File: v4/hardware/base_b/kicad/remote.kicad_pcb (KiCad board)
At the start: 2 copper layers, 111.8 x 100.3 mm, 31 parts, among them J12 Conn_01x04_Female, J16 Conn_01x04_Female, J19 Conn_01x03_Female, J2 Conn_01x12_Female, J20 Conn_01x04_Female, J3 Conn_01x16_Female, J5 Conn_01x03_Female, Q1 Q_NMOS_GDS, Q3 Q_NPN_EBC, SW1 SW_Push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

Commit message: update
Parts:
- removed J2: Conn_01x12_Female, Connector_PinSocket_2.54mm:PinSocket_1x12_P2.54mm_Vertical
- removed J3: Conn_01x16_Female, Connector_PinSocket_2.54mm:PinSocket_1x16_P2.54mm_Vertical
- removed gps1: Conn_01x04_Female, footprints:gps_neo6_blue_0
- removed sharp1: Conn_01x09_Female, footprints:Display_adafruit_sharp_13
- added AE1: Antenna_Shield, Connector_Coaxial:SMA_Amphenol_132289_EdgeMount, F.Cu at (-16.5, -20.3)
- added R7: 4.7K, Resistor_THT:R_Axial_DIN0309_L9.0mm_D3.2mm_P12.70mm_Horizontal, F.Cu at (44.5, 20.3)
- added SW3: SW_Push, Button_Switch_THT:SW_Tactile_SPST_Angled_PTS645Vx58-2LFS, F.Cu at (17.8, 8.89)
- added U3: Adafruit_IMU_BNO005, footprints:IMU_Ada_BNO005, F.Cu at (-16.5, 3.81)
- added U4: Adafruit_Sharp_Display_1_3, footprints:Display_adafruit_sharp_13, F.Cu at (0.00, 41.9)
- added U5: neo-6m-black, footprints:gps_neo6m_black, F.Cu at (-15.2, 36.8)
- moved H6 190.8 mm to (-27.9, -19.1)
- moved J5 164.4 mm to (-29.2, 14.0)
- moved H2 155.5 mm to (17.8, -19.1)
- moved H1 135.7 mm to (-29.2, 72.4)
- moved SW1 134.3 mm to (17.8, -11.4), turned to 270 degrees
- moved SW2 125.2 mm to (17.8, -1.27), turned to 270 degrees
- moved J16 101.1 mm to (19.1, 26.7)
- moved H5 96.6 mm to (19.1, 72.4)
- moved U1 91.6 mm to (-1.27, 0.00), turned to 180 degrees
- moved U2 5.24 mm to (14.0, 47.0), turned to 270 degrees
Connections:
- J5 pad 2: EN -> (no net)
- U2 pad 11: (no net) -> SCL
- U2 pad 12: (no net) -> SDA
- U2 pad 17: (no net) -> A0
- U2 pad 20: (no net) -> A3
- U2 pad 21: (no net) -> A4
- U2 pad 22: (no net) -> A5
- U2 pad 26: (no net) -> RX_D0
- U2 pad 27: (no net) -> TX_D1
- U2 pad 28: (no net) -> DW
- U2 pad 8: (no net) -> D9
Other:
- board size 111.8 x 100.3 mm -> 53.3 x 97.8 mm

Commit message: update
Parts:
- removed AE1: Antenna_Shield, Connector_Coaxial:SMA_Amphenol_132289_EdgeMount
- added J1: Conn_Coaxial, Connector_Coaxial:SMA_Amphenol_132134_Vertical, F.Cu at (-14.0, -21.6)
- moved J20 176.5 mm to (-27.9, -1.27), turned to 270 degrees
- moved J12 172.8 mm to (-27.9, -11.4), turned to 270 degrees
- moved J19 154.6 mm to (-21.6, 72.4), turned to 90 degrees
- moved SP1 149.9 mm to (7.62, -8.89), turned to 90 degrees
- moved SW4 138.4 mm to (-30.5, 35.6), turned to 90 degrees
- moved R4 129.9 mm to (-24.1, 63.5), turned to 90 degrees
- moved R6 119.1 mm to (-29.2, 63.5), turned to 90 degrees
- moved R3 115.0 mm to (-8.89, 63.5), turned to 90 degrees
- moved Q3 113.1 mm to (19.1, 39.4), turned to 180 degrees
- moved JP1 104.7 mm to (6.74, 26.3), turned to 270 degrees
- moved JP3 103.7 mm to (6.74, 22.0), turned to 270 degrees
- moved R8 102.1 mm to (-19.1, 63.5), turned to 90 degrees
- moved Q1 96.2 mm to (19.1, 31.8), turned to 180 degrees
- moved R2 90.1 mm to (-14.0, 63.5), turned to 90 degrees
- moved R1 89.7 mm to (-3.81, 63.5), turned to 90 degrees
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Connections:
- U1 pad 9: (no net) -> Net-(J1-Pad1)
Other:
- board size 53.3 x 97.8 mm -> 53.3 x 100.3 mm

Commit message: update
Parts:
- removed J12: Conn_01x04_Female, Connector_JST:JST_SH_SM04B-SRSS-TB_1x04-1MP_P1.00mm_Horizontal
- removed JP3: Jumper_NO_Small, Jumper:SolderJumper-2_P1.3mm_Open_Pad1.0x1.5mm
- added J2: Conn_01x06_Female, Connector_PinHeader_2.54mm:PinHeader_1x06_P2.54mm_Vertical, F.Cu at (-26.5, 19.1)
- added J3: Conn_01x04_Female, Connector_JST:JST_SH_SM04B-SRSS-TB_1x04-1MP_P1.00mm_Horizontal, F.Cu at (-28.1, -11.9)
- added JP2: Jumper_NO_Small, Jumper:SolderJumper-2_P1.3mm_Open_Pad1.0x1.5mm, B.Cu at (-21.5, -1.14)
- Q1: footprint Package_TO_SOT_THT:TO-220-3_Vertical -> Package_TO_SOT_THT:TO-220-3_Horizontal_TabDown
- moved Q3 63.9 mm to (-8.22, -18.4), turned to 90 degrees
- moved J5 50.4 mm to (19.4, 27.0)
- moved SW4 42.0 mm to (-14.7, 74.5), turned to 180 degrees
- moved J16 34.0 mm to (-14.3, 7.56), turned to 90 degrees
- moved Q1 31.6 mm to (5.52, 3.24), turned to 0 degrees
- moved J19 20.7 mm to (-0.98, 73.8), turned to 270 degrees
- moved SP1 15.7 mm to (-2.72, -20.7), turned to 270 degrees
- moved H2 10.1 mm to (17.8, -21.6)
- moved SW1 8.12 mm to (18.3, -13.7)
- moved SW2 8.12 mm to (18.3, -3.52)
- moved SW3 8.12 mm to (18.3, 6.64)
- moved R6 6.35 mm to (-22.9, 63.5)
- moved R4 5.41 mm to (-18.7, 63.5)
- moved R8 4.46 mm to (-14.6, 63.5)
- moved R2 3.52 mm to (-10.5, 63.5)
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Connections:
- J19 pad 3: A3 -> A5
- J5 pad 2: (no net) -> EN
- R3 pad 2: A5 -> A3
- R4 pad 2: A4 -> A2
- R7 pad 2: A2 -> A4
- R8 pad 2: A0 -> A1
- SW1 pad 1: A4 -> A2
- SW2 pad 1: A5 -> A3
- SW3 pad 1: A2 -> A4
- U1 pad 14: (no net) -> D9
- U1 pad 15: (no net) -> Net-(JP2-Pad1)
- U1 pad 2: (no net) -> MISO
- U1 pad 3: (no net) -> MOSI
- U1 pad 4: (no net) -> SCK
- U1 pad 5: (no net) -> D5
- U1 pad 6: (no net) -> D6
- U2 pad 10: (no net) -> D5
- U2 pad 13: (no net) -> ~RESET
- U2 pad 14: (no net) -> +3V3
- U2 pad 16: (no net) -> GND
- U2 pad 18: (no net) -> A1
- U2 pad 19: (no net) -> A2
- U2 pad 2: (no net) -> EN
- U2 pad 23: (no net) -> SCK
- U2 pad 24: (no net) -> MOSI
- U2 pad 25: (no net) -> MISO
- U2 pad 28: DW -> (no net)
- U2 pad 4: (no net) -> D13
- U2 pad 5: (no net) -> D12
- U2 pad 6: (no net) -> D11
- U2 pad 7: (no net) -> D10
- U2 pad 9: (no net) -> D6
- U4 pad 4: (no net) -> SCK
- U4 pad 5: (no net) -> MOSI
- U4 pad 6: (no net) -> A0
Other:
- board size 53.3 x 100.3 mm -> 53.3 x 115.3 mm
- board text added: "JST"

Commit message: update
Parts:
- JP1: moved to B.Cu
- moved J3 69.6 mm to (-28.2, 57.7)
- moved Q3 58.0 mm to (-26.9, 36.6)
- moved R1 23.2 mm to (-21.7, 50.9), turned to 270 degrees
- moved R4 17.3 mm to (-1.43, 63.6)
- moved R8 17.2 mm to (2.63, 63.6)
- moved R2 14.5 mm to (-17.7, 50.9), turned to 270 degrees
- moved SP1 13.3 mm to (10.6, -21.0), turned to 180 degrees
- moved JP2 11.5 mm to (-10.4, -4.26), turned to 90 degrees
- moved R7 11.5 mm to (-9.55, 63.6)
- moved R6 9.26 mm to (-13.6, 63.6)
- moved U3 6.30 mm to (-23.7, 1.96)
- moved J20 5.69 mm to (-28.3, -7.11)
- moved SW2 4.91 mm to (15.3, 0.39)
- moved SW3 4.75 mm to (15.3, 10.4)
- moved J2 4.21 mm to (-27.5, 15.0)
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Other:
- outline, holes or cut-outs redrawn

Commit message: update
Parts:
- moved D2 12.7 mm to (11.8, 51.5), turned to 270 degrees
- moved SP1 3.77 mm to (6.82, -20.9)
- moved SW1 0.25 mm to (15.1, -13.4)
- moved SW2 0.23 mm to (15.1, 0.39)
- moved SW3 0.23 mm to (15.1, 10.4)
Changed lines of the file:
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@@
   )
   (module Button_Switch_THT:SW_Tactile_SPST_Angled_PTS645Vx58-2LFS (layer F.Cu)
-    (at 15.33144 10.3505 270)
+    (at 15.10538 10.3505 270)
     (descr "tactile switch SPST right angle, PTS645VL58-2 LFS")
     (tags "tactile switch SPST angled PTS645VL58-2 LFS C&K Button")
@@
   )
   (module Button_Switch_THT:SW_Tactile_SPST_Angled_PTS645Vx58-2LFS (layer F.Cu)
-    (at 15.33144 0.3937 270)
+    (at 15.10538 0.3937 270)
     (descr "tactile switch SPST right angle, PTS645VL58-2 LFS")
     (tags "tactile switch SPST angled PTS645VL58-2 LFS C&K Button")
@@
   )
   (module Button_Switch_THT:SW_Tactile_SPST_Angled_PTS645Vx58-2LFS (layer F.Cu)
-    (at 15.3543 -13.41628 270)
+    (at 15.10538 -13.41628 270)
     (descr "tactile switch SPST right angle, PTS645VL58-2 LFS")
     (tags "tactile switch SPST angled PTS645VL58-2 LFS C&K Button")
@@
   )
   (module "Adafruit Circuit Playground:BUZZER_SMT_5MM" (layer F.Cu)
-    (at 10.58926 -20.98802 180)
+    (at 6.81736 -20.8788 180)
     (fp_text reference SP1 (at 0 0) (layer F.SilkS) hide
       (effects (font (size 1.27 1.27) (thickness 0.15)))
@@
   )
   (module Diode_THT:D_5W_P12.70mm_Horizontal (layer F.Cu)
-    (at 11.71702 64.20612 90)
+    (at 11.81354 51.51374 270)
     (descr "Diode, 5W series, Axial, Horizontal, pin pitch=12.7mm, , length*diameter=8.9*3.7mm^2, , http://www.diodes.com/_files/packages/8686949.gif")
     (tags "Diode 5W series Axial Horizontal pin pitch 12.7mm  length 8.9mm diameter 3.7mm")
@@
     (fp_line (start 14.35 2.1) (end 14.35 -2.1) (layer F.CrtYd) (width 0.05))
     (fp_line (start 14.35 -2.1) (end -1.65 -2.1) (layer F.CrtYd) (width 0.05))
-    (pad 1 thru_hole rect (at 0 0 90) (size 2.8 2.8) (drill 1.4) (layers *.Cu *.Mask)
+    (pad 1 thru_hole rect (at 0 0 270) (size 2.8 2.8) (drill 1.4) (layers *.Cu *.Mask)
       (net 3 +3V3))
-    (pad 2 thru_hole oval (at 12.7 0 90) (size 2.8 2.8) (drill 1.4) (layers *.Cu *.Mask)
+    (pad 2 thru_hole oval (at 12.7 0 270) (size 2.8 2.8) (drill 1.4) (layers *.Cu *.Mask)
       (net 2 "Net-(D2-Pad2)"))
     (model ${KISYS3DMOD}/Diode_THT.3dshapes/D_5W_P12.70mm_Horizontal.wrl

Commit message: nice board layout for v4 base_b
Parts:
- removed the R5 at (6.68, 63.6)
- removed the R6 at (-13.6, 63.6)
- added R3: 10K, Resistor_THT:R_Axial_DIN0309_L9.0mm_D3.2mm_P12.70mm_Horizontal, F.Cu at (-10.9, 63.9)
- moved H5 94.1 mm to (17.8, -21.8)
- moved H2 93.5 mm to (17.8, 71.9)
- moved R1 2.68 mm to (-19.1, 51.2)
- moved R4 2.68 mm to (-6.89, 63.9)
- moved R5 2.68 mm to (-2.83, 63.9)
- moved R6 2.68 mm to (1.23, 63.9)
- moved R7 2.68 mm to (5.29, 63.9)
- moved R2 2.68 mm to (-15.0, 51.2)
- moved SW1 1.87 mm to (15.2, -15.3)
- moved J2 1.40 mm to (-26.1, 14.9)
- moved SW2 1.10 mm to (15.3, -0.69)
- moved SW3 1.10 mm to (15.3, 9.27)
- moved SW4 1.03 mm to (-12.9, 74.6)
- moved D1 0.80 mm to (11.1, 51.8)
- moved J16 0.64 mm to (-14.4, 6.93)
- renumbered D2 to D1, R7 to R4, R3 to R5, R4 to R6, R8 to R7
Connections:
- J19 pad 2: Net-(J19-Pad2) -> GND
- U3 pad 1: (no net) -> +3V3
- U3 pad 3: (no net) -> GND
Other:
- outline, holes or cut-outs redrawn
- board text added: "3.7V"
- board text added: "3V"
- board text added: "3V3"
- board text added: "A"
- board text added: "A1"
- board text added: "ANT"
- board text added: "ANTENNA"
- board text added: "B"
- board text added: "C"
- board text added: "D11"
- board text added: "D12"
- board text added: "D13"
- board text added: "G1"
- board text added: "GND"
- board text added: "GPS"
- board text added: "IMU"
- board text added: "LOG"
- board text added: "OFF"
- board text added: "ON"
- board text added: "PROG"
- board text added: "RESET"
- board text added: "RFM95"
- board text added: "RX_DO"
- board text added: "SCL"
- board text added: "SDA"
- board text added: "Sharp display"
- board text added: "Sharp display breakout"
- board text added: "TX_D1"

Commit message: update
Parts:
- Q1: footprint Package_TO_SOT_THT:TO-220-3_Horizontal_TabDown -> Package_TO_SOT_THT:TO-220-3_Horizontal_TabUp
- moved Q1 4.86 mm to (7.53, 3.15), turned to 180 degrees
- moved D1 0.98 mm to (10.1, 51.9)
- moved R1 0.72 mm to (-19.8, 51.3)
- moved R2 0.72 mm to (-15.7, 51.3)
- moved R3 0.72 mm to (-11.7, 64.0)
- moved R7 0.72 mm to (4.57, 64.0)
- moved R5 0.72 mm to (-3.55, 64.0)
- moved R6 0.72 mm to (0.51, 64.0)
- moved R4 0.72 mm to (-7.61, 64.0)

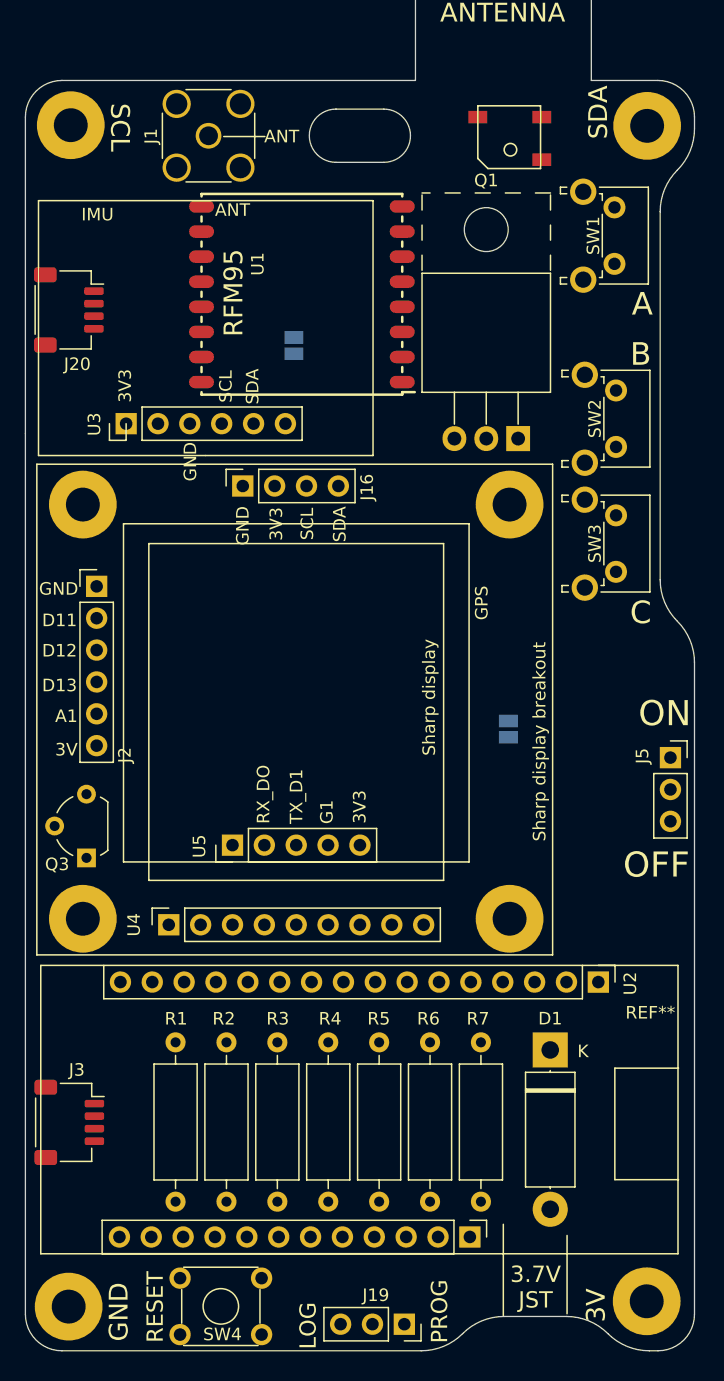
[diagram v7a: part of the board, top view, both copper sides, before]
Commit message: routed power lines
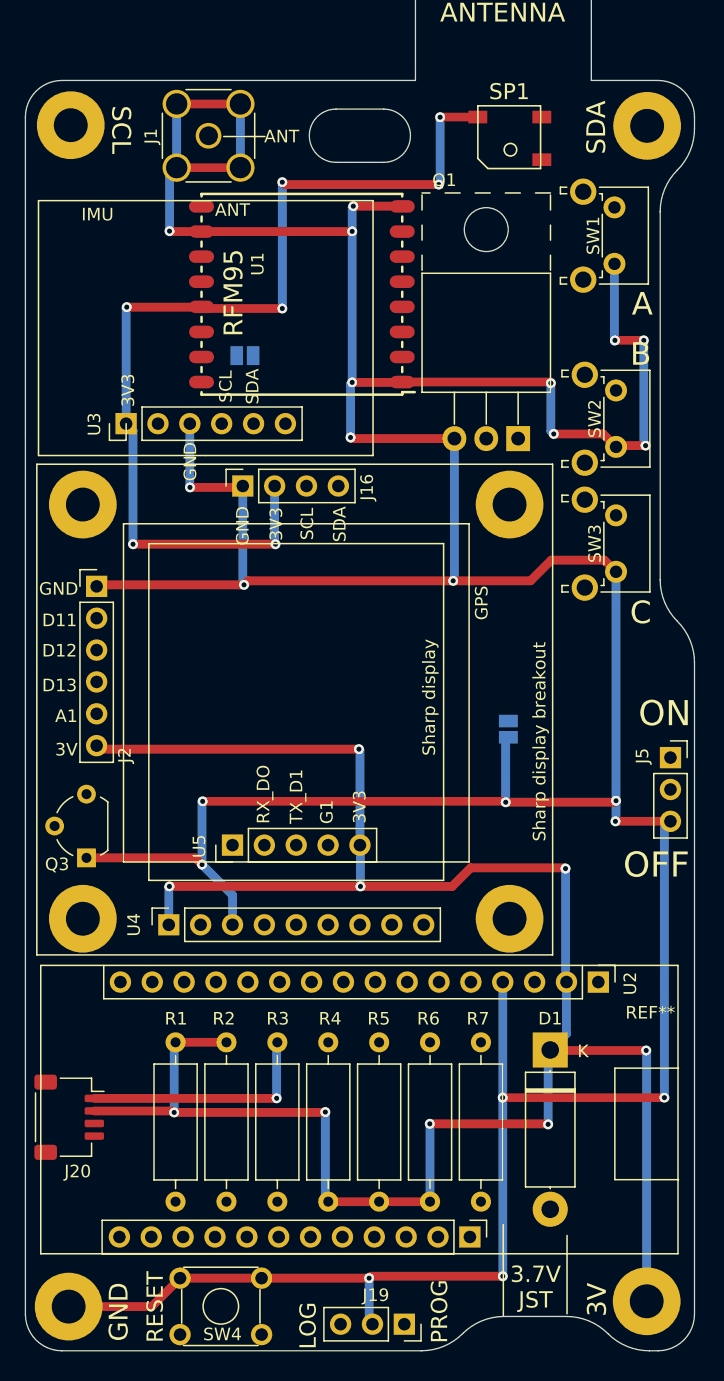
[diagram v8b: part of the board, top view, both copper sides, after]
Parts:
- removed J3: Conn_01x04_Female, Connector_JST:JST_SH_SM04B-SRSS-TB_1x04-1MP_P1.00mm_Horizontal
- moved J20 64.4 mm to (-28.3, 57.2)
- moved JP2 3.98 mm to (-14.2, -3.46), turned to 0 degrees
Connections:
- J2 pad 2: D11 -> D10
- J2 pad 3: D12 -> D13
- J2 pad 4: D13 -> A1
- J2 pad 5: A1 -> A0
- JP2 pad 2: D10 -> A0
- U1 pad 1: (no net) -> GND
- U1 pad 10: (no net) -> GND
- U1 pad 13: (no net) -> +3V3
- U1 pad 14: D9 -> D12
- U1 pad 5: D5 -> D11
- U1 pad 8: (no net) -> GND
- U4 pad 6: A0 -> D5
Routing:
- net GND: track 0.00 -> 386.9 mm, vias 0 -> 23
- net +3V3: track 0.00 -> 253.9 mm, vias 0 -> 16
